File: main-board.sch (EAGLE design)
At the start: 53 parts, among them IC1 MEGA328-PB, IC2 MCP73831, IC3 LE33, Q1 3,6864 MHz, Q4 TSM2302CX, T1 IRF7306

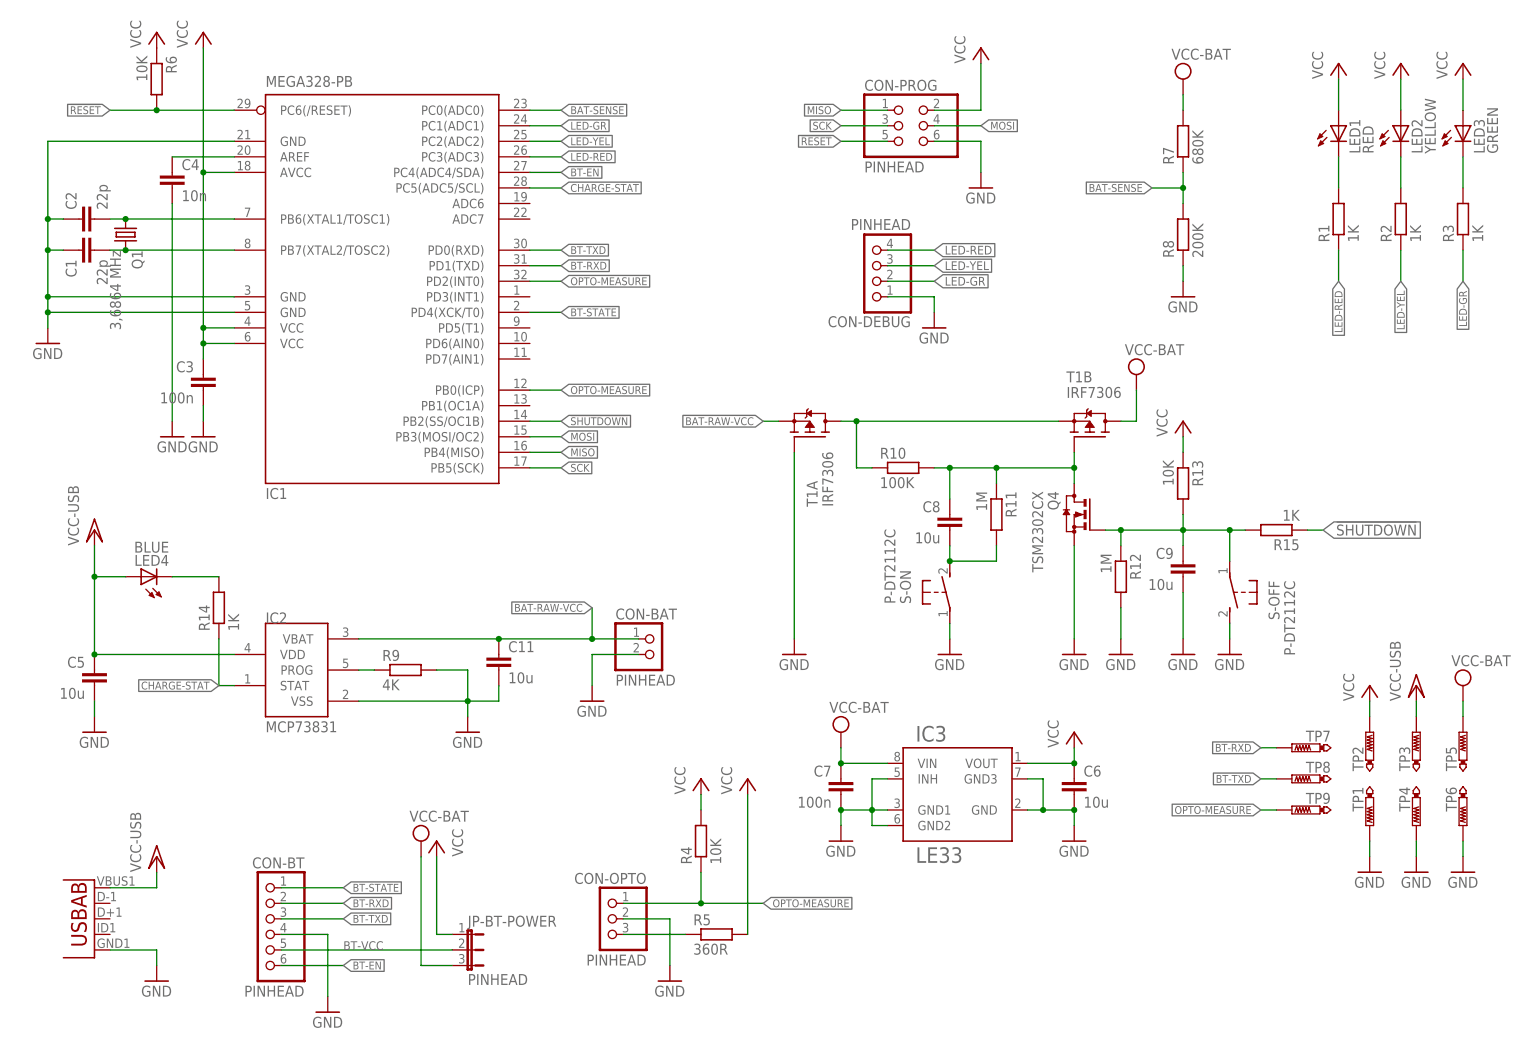
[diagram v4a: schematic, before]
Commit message: Schematics: move power parts together.
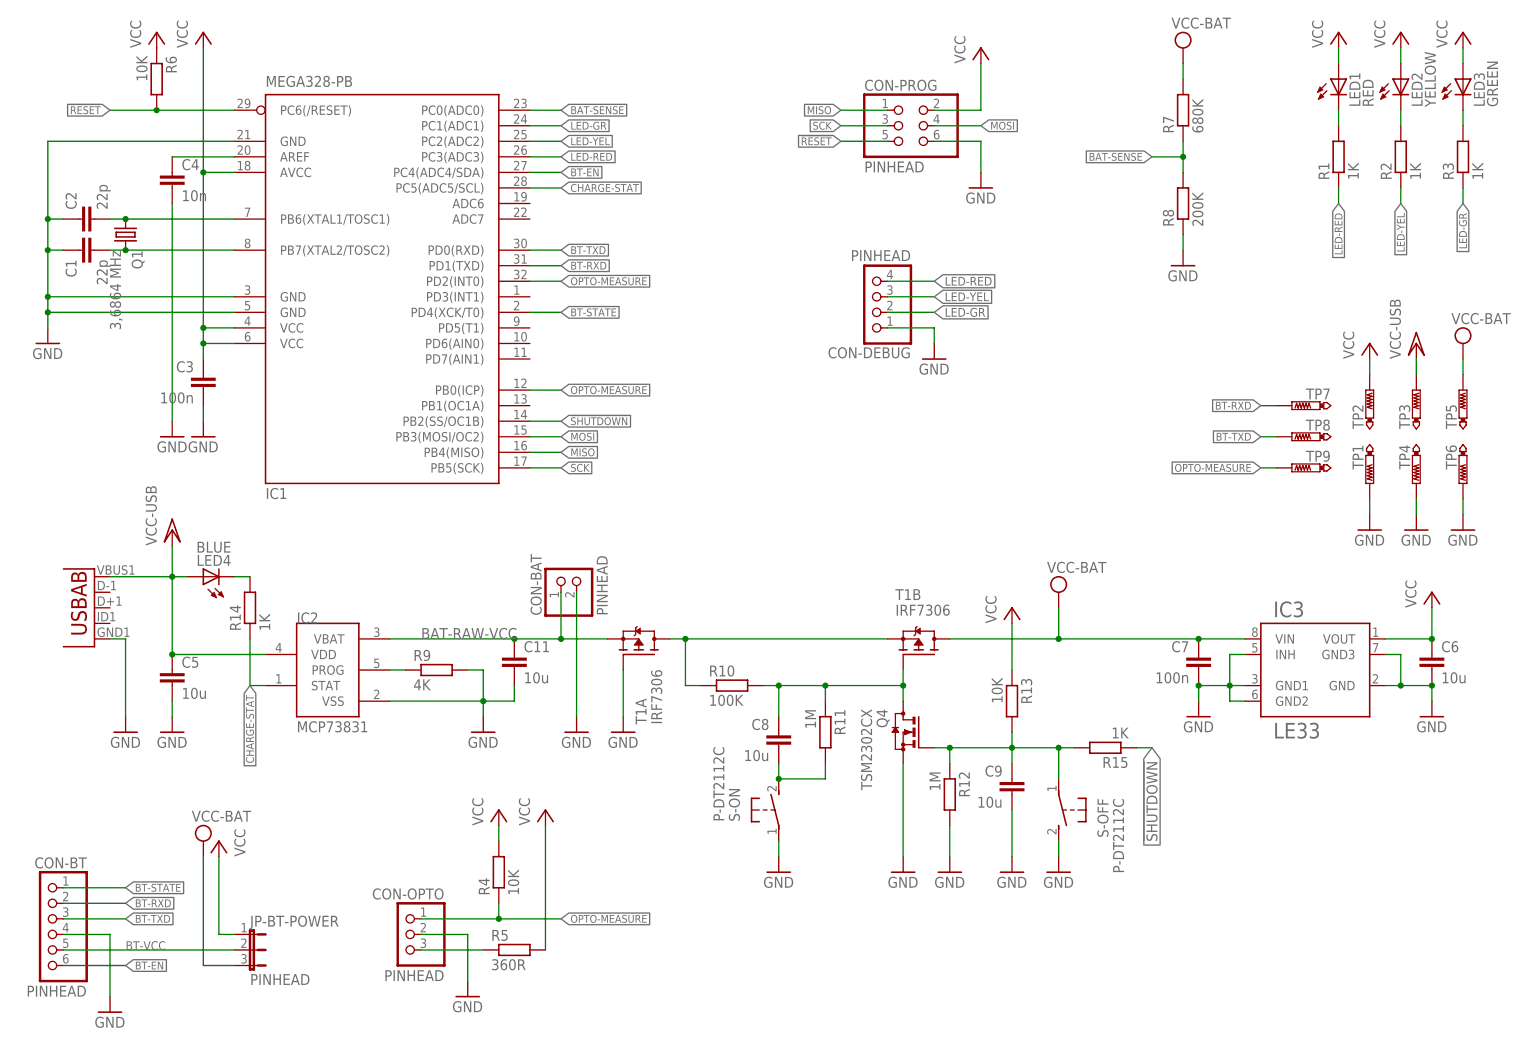
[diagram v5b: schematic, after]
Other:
- moved on the sheet: C11, C5, C6, C7, C8, C9, CON-BAT, CON-BT, CON-DEBUG, CON-OPTO, IC2, IC3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

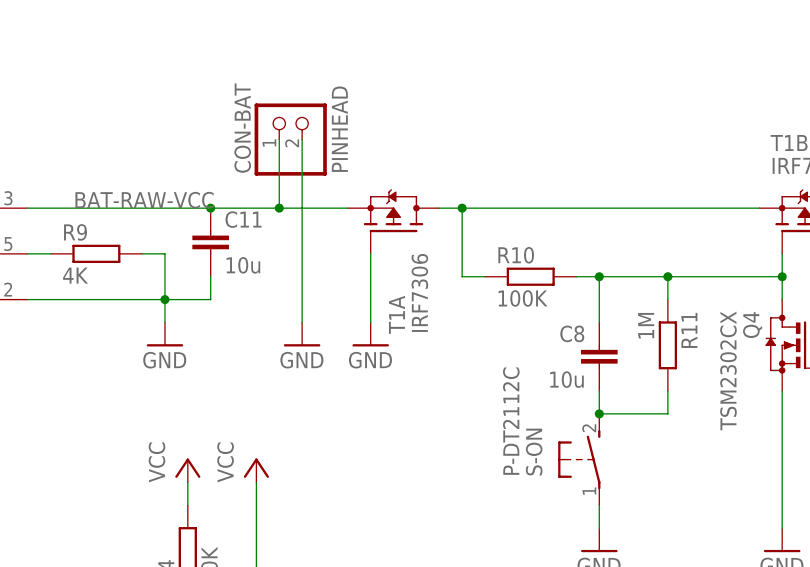
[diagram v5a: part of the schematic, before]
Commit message: Fix polarity-protection MOSFET.
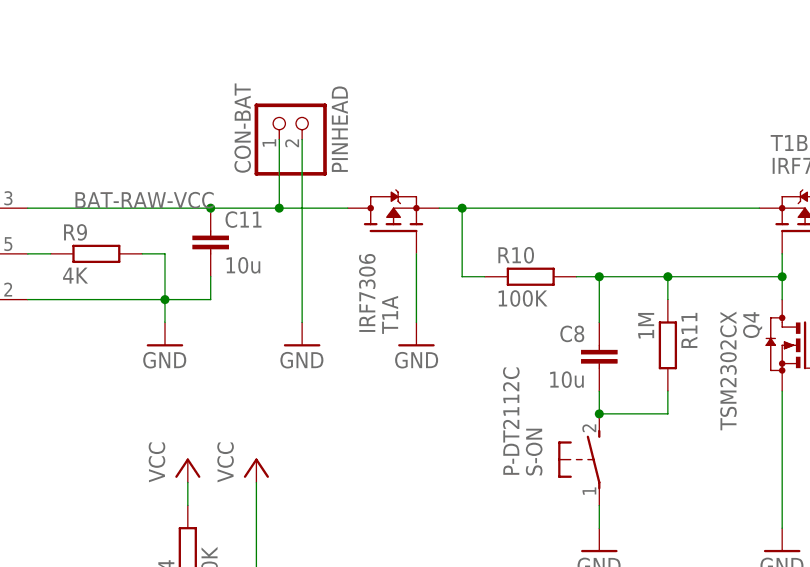
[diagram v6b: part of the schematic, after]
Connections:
- net BAT-POS-VCC: now also T1A.S; no longer T1A.D
- net BAT-RAW-VCC: now also T1A.D; no longer T1A.S
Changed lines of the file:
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@@
 <instance part="CON-DEBUG" gate="A" x="147.32" y="127" rot="R180"/>
 <instance part="GND17" gate="1" x="157.48" y="116.84"/>
-<instance part="T1" gate="A" x="109.22" y="68.58" rot="R90"/>
+<instance part="T1" gate="A" x="109.22" y="68.58" rot="MR90"/>
 <instance part="T1" gate="B" x="154.94" y="68.58" smashed="yes" rot="R90">
 <attribute name="VALUE" x="151.13" y="74.93" size="1.778" layer="96"/>
 <attribute name="NAME" x="151.13" y="77.47" size="1.778" layer="95"/>
 </instance>
-<instance part="GND18" gate="1" x="106.68" y="55.88"/>
+<instance part="GND18" gate="1" x="111.76" y="55.88" rot="MR0"/>
 <instance part="P+13" gate="VCC" x="93.98" y="43.18"/>
 <instance part="JP-BT-POWER" gate="1" x="45.72" y="20.32" rot="R270"/>
@@
 <pinref part="GND18" gate="1" pin="GND"/>
 <pinref part="T1" gate="A" pin="G"/>
-<wire x1="106.68" y1="58.42" x2="106.68" y2="66.04" width="0.1524" layer="91"/>
+<wire x1="111.76" y1="58.42" x2="111.76" y2="66.04" width="0.1524" layer="91"/>
 </segment>
 </net>
@@
 <net name="BAT-RAW-VCC" class="1">
 <segment>
-<pinref part="T1" gate="A" pin="S"/>
 <pinref part="CON-BAT" gate="G$1" pin="1"/>
 <wire x1="96.52" y1="71.12" x2="96.52" y2="78.74" width="0.1524" layer="91"/>
@@
 <junction x="88.9" y="71.12"/>
 <label x="73.66" y="71.12" size="1.778" layer="95"/>
+<pinref part="T1" gate="A" pin="D"/>
 <wire x1="104.14" y1="71.12" x2="96.52" y2="71.12" width="0.1524" layer="91"/>
 <junction x="96.52" y="71.12"/>
@@
 <wire x1="116.84" y1="63.5" x2="116.84" y2="71.12" width="0.1524" layer="91"/>
 <wire x1="116.84" y1="71.12" x2="149.86" y2="71.12" width="0.1524" layer="91"/>
+<pinref part="T1" gate="B" pin="S"/>
+<pinref part="T1" gate="A" pin="S"/>
+<wire x1="116.84" y1="71.12" x2="114.3" y2="71.12" width="0.1524" layer="91"/>
 <junction x="116.84" y="71.12"/>
-<pinref part="T1" gate="B" pin="S"/>
-<pinref part="T1" gate="A" pin="D"/>
-<wire x1="114.3" y1="71.12" x2="116.84" y2="71.12" width="0.1524" layer="91"/>
-</segment>
-</net>
+</segment>
+</net>

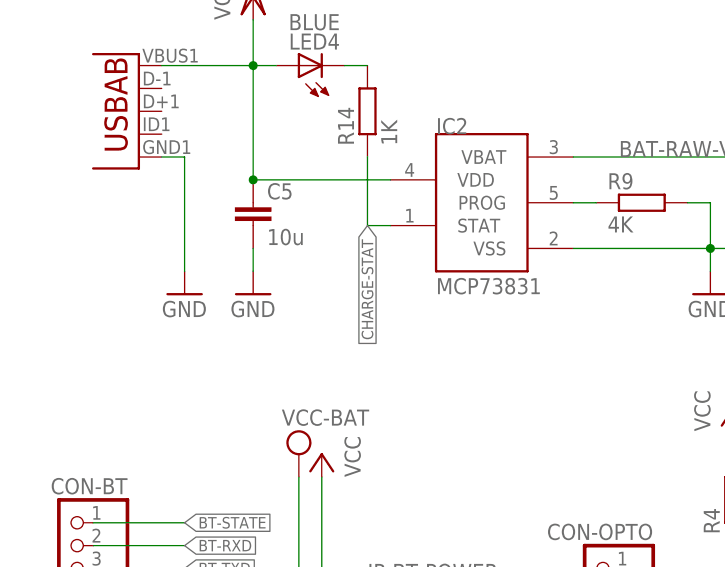
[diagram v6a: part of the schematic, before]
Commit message: Add diode to CHARGE-STAT pin.
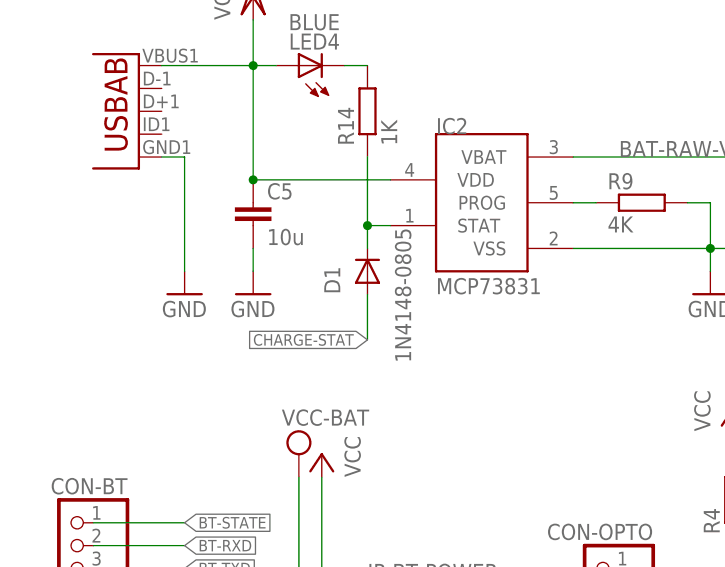
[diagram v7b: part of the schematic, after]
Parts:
- added D1: 1N4148-0805, diode:1N4148-0805
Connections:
- new net CHARGE-STAT-INT: D1.C, IC2.STAT, R14.1
- net CHARGE-STAT: now also D1.A; no longer IC2.STAT, R14.1
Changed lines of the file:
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@@
 <part name="S-OFF" library="switch-tact" deviceset="DTSM-3" device="" value="P-DT2112C"/>
 <part name="SUPPLY4" library="supply2" deviceset="VCC" device="" value="VCC-BAT"/>
+<part name="D1" library="diode" deviceset="1N4148" device="-0805"/>
 </parts>
 <sheets>
@@
 </instance>
 <instance part="SUPPLY4" gate="G$1" x="38.1" y="38.1"/>
+<instance part="D1" gate="A" x="45.72" y="58.42" smashed="yes" rot="R90">
+<attribute name="NAME" x="42.6974" y="55.88" size="1.778" layer="95" rot="R90"/>
+<attribute name="VALUE" x="50.5714" y="48.26" size="1.778" layer="96" rot="R90"/>
+</instance>
 </instances>
 <busses>
@@
 <net name="CHARGE-STAT" class="0">
 <segment>
-<pinref part="IC2" gate="G$1" pin="STAT"/>
-<wire x1="48.26" y1="63.5" x2="45.72" y2="63.5" width="0.1524" layer="91"/>
-<label x="45.72" y="63.5" size="1.27" layer="95" rot="R270" xref="yes"/>
-<pinref part="R14" gate="G$1" pin="1"/>
-<wire x1="45.72" y1="63.5" x2="45.72" y2="71.12" width="0.1524" layer="91"/>
-</segment>
-<segment>
 <label x="96.52" y="144.78" size="1.27" layer="95" xref="yes"/>
 <pinref part="IC1" gate="G$1" pin="PC5(ADC5/SCL)"/>
 <wire x1="96.52" y1="144.78" x2="91.44" y2="144.78" width="0.1524" layer="91"/>
+</segment>
+<segment>
+<pinref part="D1" gate="A" pin="A"/>
+<wire x1="45.72" y1="55.88" x2="45.72" y2="50.8" width="0.1524" layer="91"/>
+<label x="45.72" y="50.8" size="1.27" layer="95" rot="R180" xref="yes"/>
 </segment>
 </net>
@@
 </segment>
 </net>
+<net name="CHARGE-STAT-INT" class="0">
+<segment>
+<pinref part="IC2" gate="G$1" pin="STAT"/>
+<wire x1="48.26" y1="63.5" x2="45.72" y2="63.5" width="0.1524" layer="91"/>
+<pinref part="R14" gate="G$1" pin="1"/>
+<wire x1="45.72" y1="63.5" x2="45.72" y2="71.12" width="0.1524" layer="91"/>
+<wire x1="45.72" y1="63.5" x2="45.72" y2="60.96" width="0.1524" layer="91"/>
+<junction x="45.72" y="63.5"/>
+<pinref part="D1" gate="A" pin="C"/>
+</segment>
+</net>

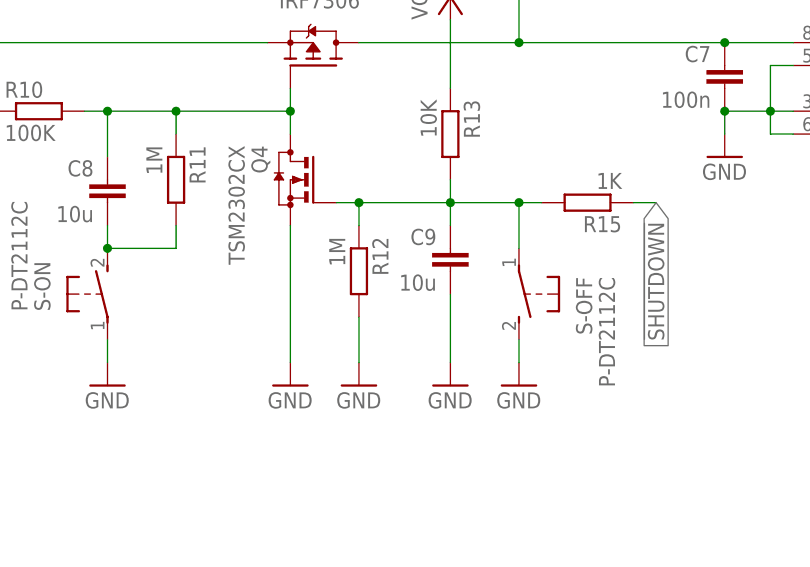
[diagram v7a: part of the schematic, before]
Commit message: Change value of C9.
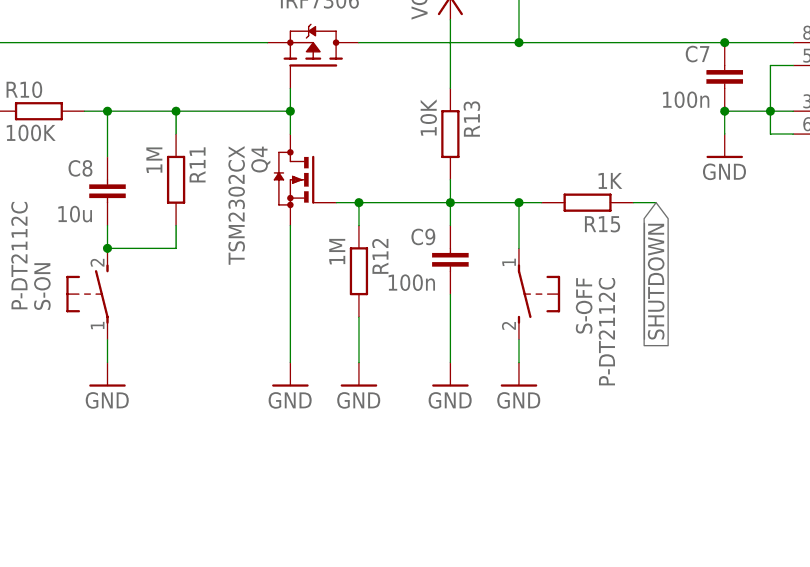
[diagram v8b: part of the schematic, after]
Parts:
- C9: value 10u -> 100n
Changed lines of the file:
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@@
 <part name="R12" library="rcl" deviceset="R-EU_" device="R0805" value="1M"/>
 <part name="R13" library="rcl" deviceset="R-EU_" device="R0805" value="10K"/>
-<part name="C9" library="rcl" deviceset="C-EU" device="C0805" value="10u"/>
+<part name="C9" library="rcl" deviceset="C-EU" device="C0805" value="100n"/>
 <part name="R10" library="rcl" deviceset="R-EU_" device="R0805" value="100K"/>
 <part name="Q4" library="transistor-small-signal" deviceset="BSS123" device="" value="TSM2302CX"/>
